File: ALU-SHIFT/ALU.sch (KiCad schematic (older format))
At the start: 55 parts, among them J1 Conn_01x02, J2 Conn_01x08, J3 Conn_01x08, J4 Conn_01x08, J5 Conn_01x04, J6 Conn_01x08, J7 Conn_01x02, U1 74LS08, U10 74LS245, U2 74LS245, U3 74LS08, U4 74LS32, U5 74LS86, U6 74LS245, U7 74LS32, U8 74LS245, U9 74LS86

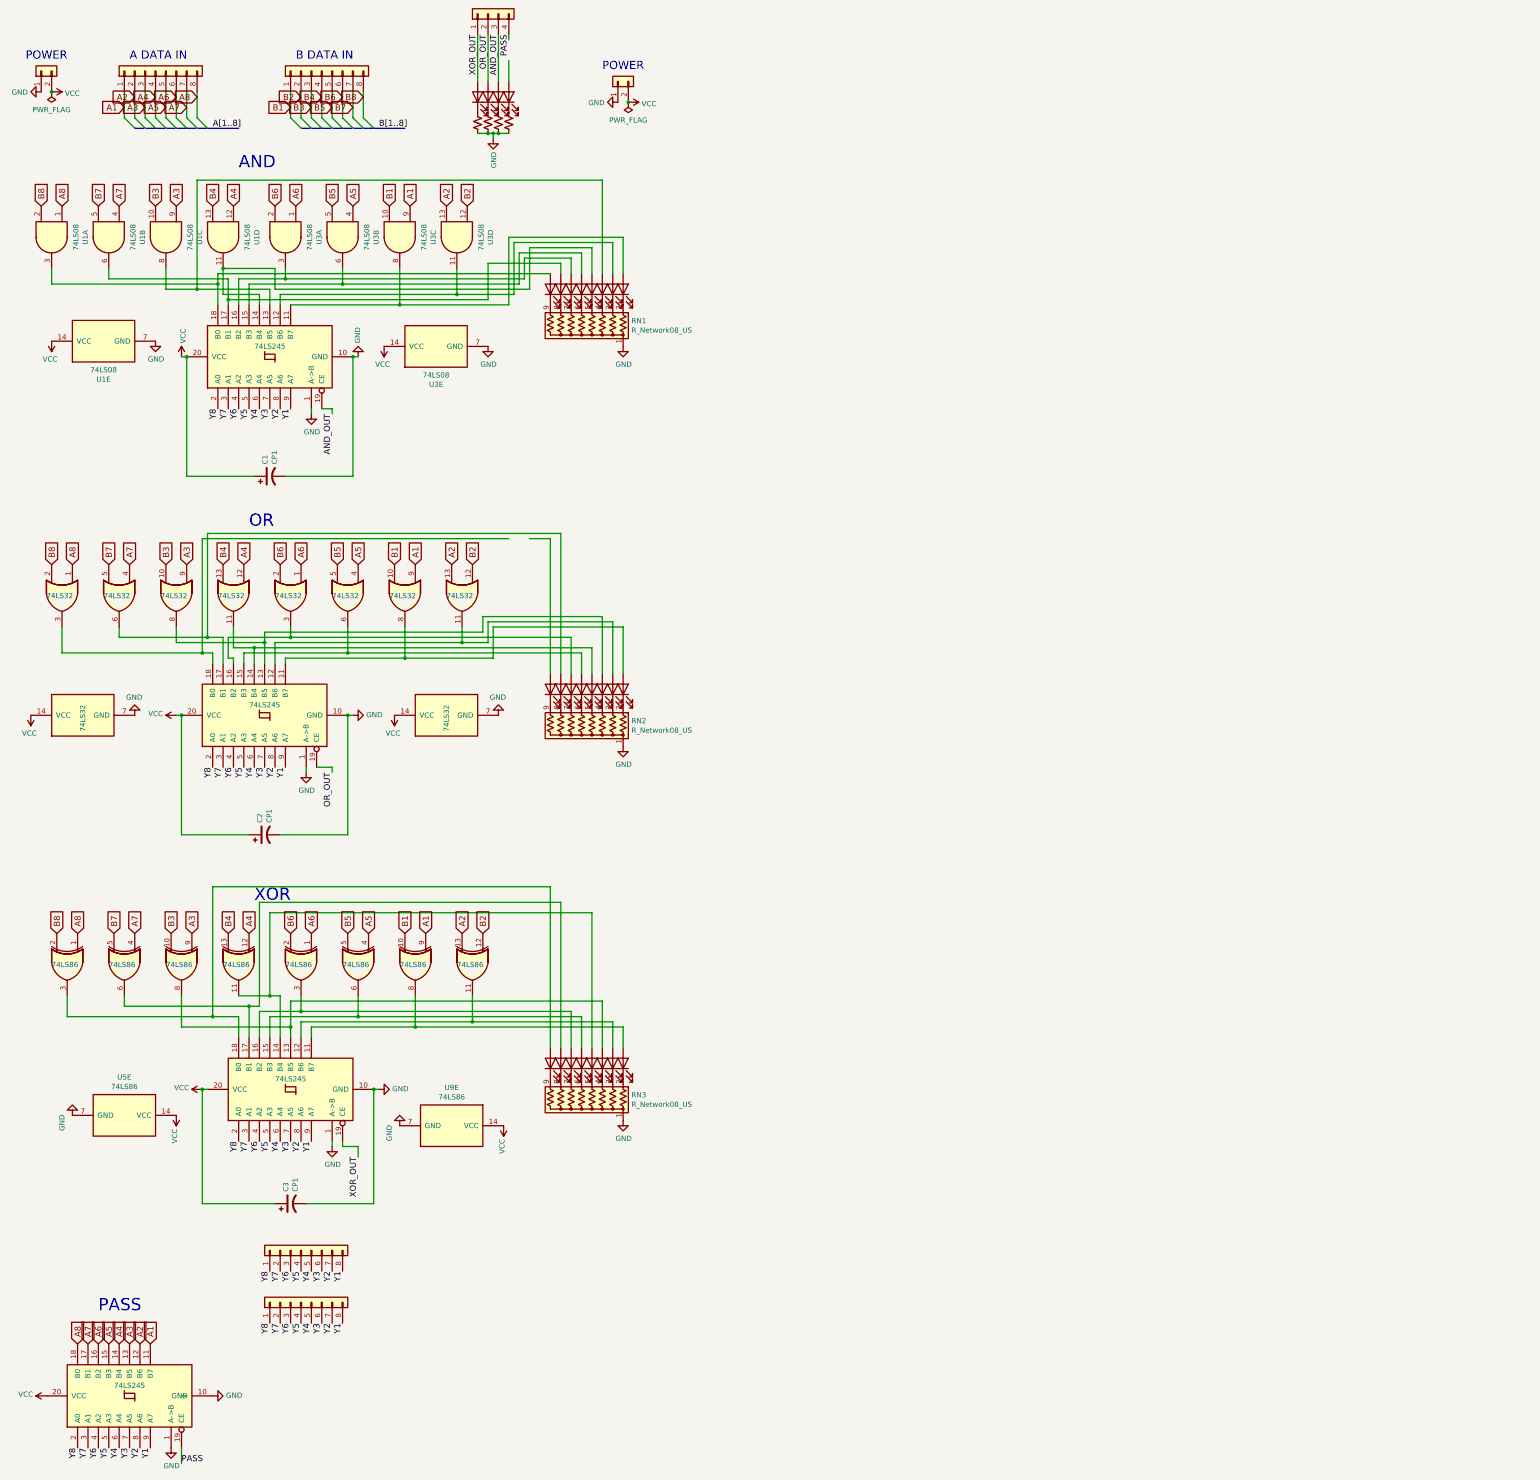
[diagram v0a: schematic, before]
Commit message: BiDirectional Shift Register component
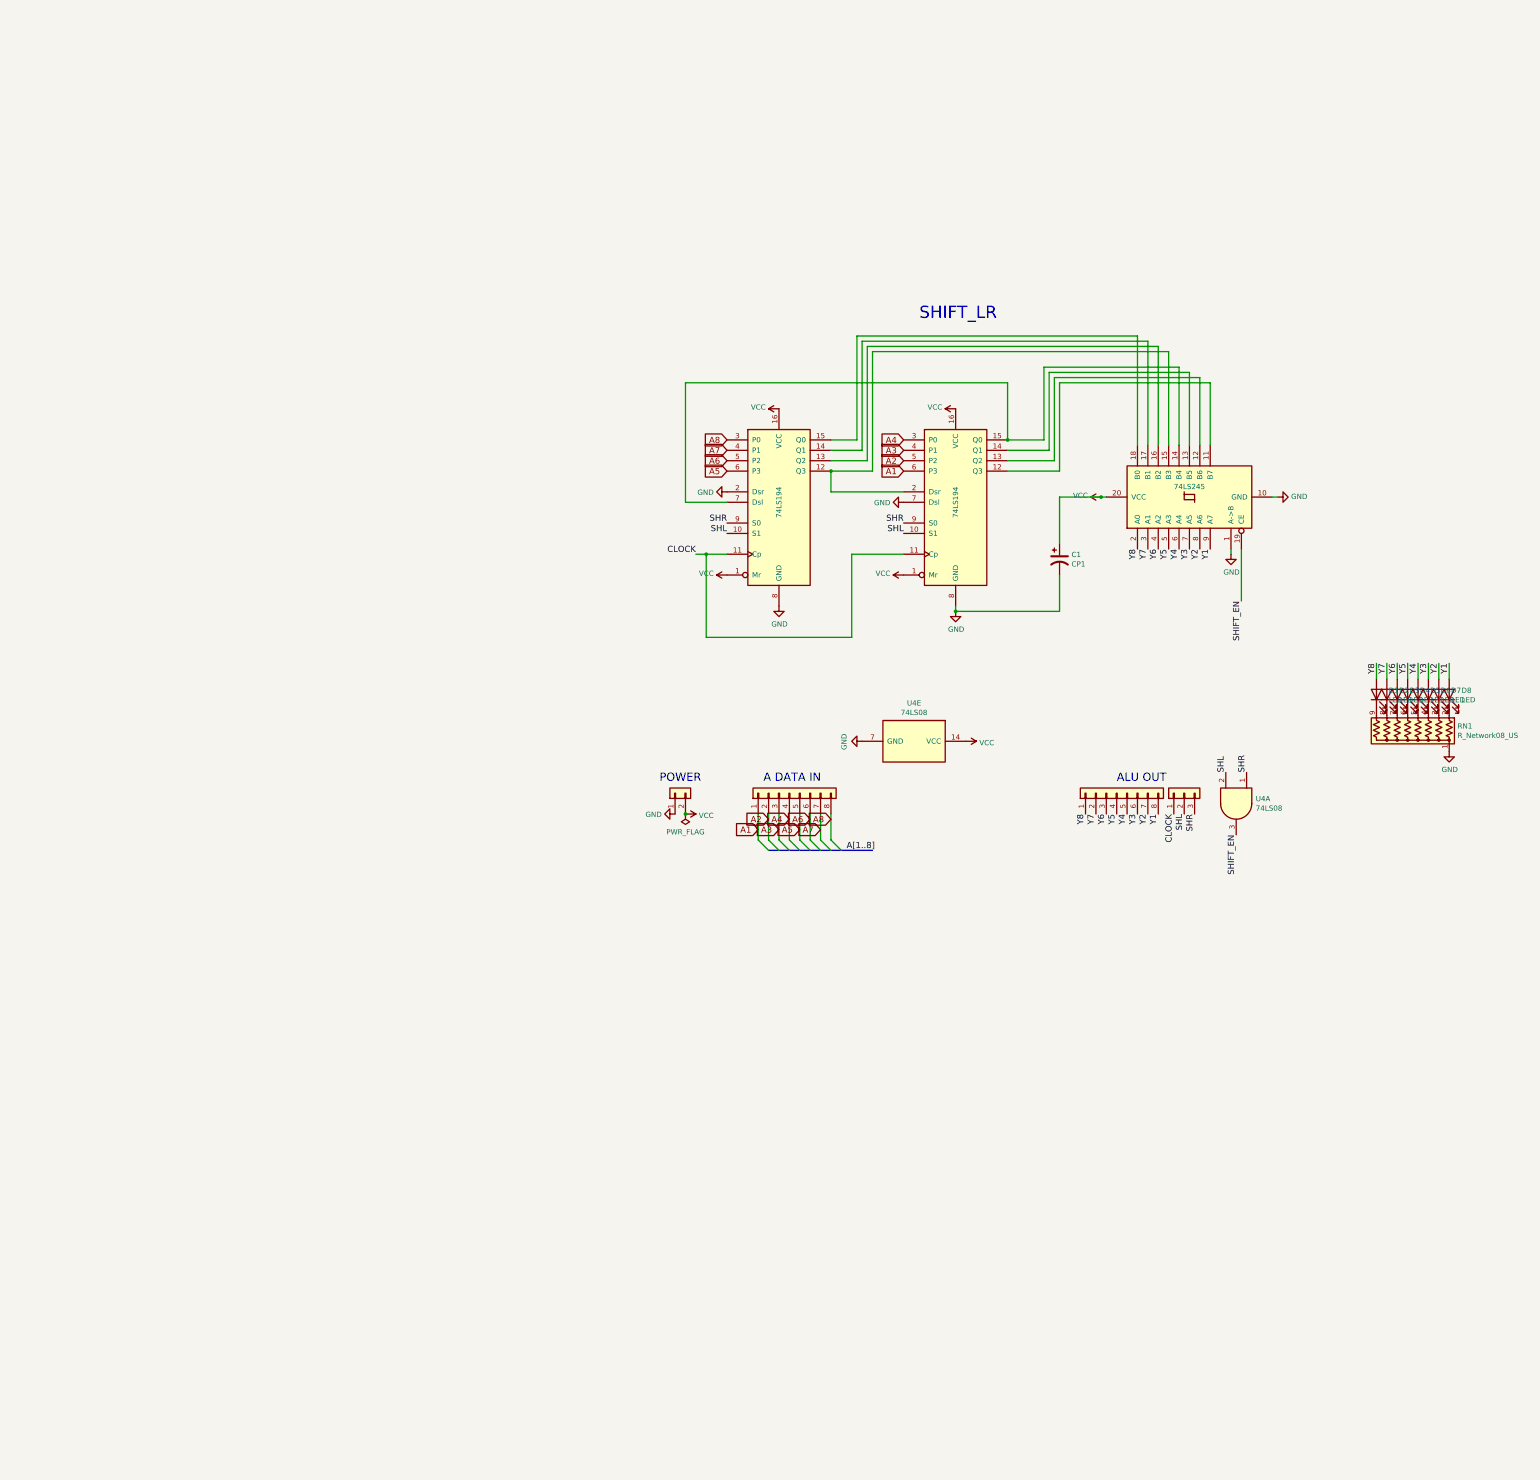
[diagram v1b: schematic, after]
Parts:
- removed C2, C3: CP1, Capacitor_THT:C_Radial_D6.3mm_H11.0mm_P2.50mm, symbol Device:CP1
- removed D10, D11, D12, D13, D14, D15, D16, D17, D18, D19, D20, D21, D22, D23, D24, D25, D26, D27, D28, D9: LED, LED_THT:LED_D5.0mm, symbol Device:LED
- removed J4, J6: Conn_01x08, Connector_PinHeader_2.54mm:PinHeader_1x08_P2.54mm_Vertical, symbol Connector_Generic:Conn_01x08
- removed J5: Conn_01x04, Connector_PinHeader_2.54mm:PinHeader_1x04_P2.54mm_Vertical, symbol Connector_Generic:Conn_01x04
- removed J7: Conn_01x02, Connector_PinHeader_2.54mm:PinHeader_1x02_P2.54mm_Vertical, symbol Connector_Generic:Conn_01x02
- removed R1, R2, R3, R4: R_Small_US, Resistor_THT:R_Axial_DIN0207_L6.3mm_D2.5mm_P10.16mm_Horizontal, symbol Device:R_Small_US
- removed RN2, RN3: R_Network08_US, Resistor_THT:R_Array_SIP9, symbol Device:R_Network08_US
- removed U1, U3: 74LS08, Package_DIP:DIP-14_W7.62mm, symbol 74xx:74LS08
- removed U10, U2, U6, U8: 74LS245, Package_DIP:DIP-20_W7.62mm, symbol 74xx:74LS245
- removed U4, U7: 74LS32, Package_DIP:DIP-14_W7.62mm, symbol 74xx:74LS32
- removed U5, U9: 74LS86, Package_DIP:DIP-14_W7.62mm, symbol 74xx:74LS86
- added J4: Conn_01x03, Connector_PinHeader_2.54mm:PinHeader_1x03_P2.54mm_Vertical, symbol Connector_Generic:Conn_01x03
- added U1, U2: 74LS194, Package_DIP:DIP-16_W7.62mm, symbol 74xx:74LS194
- added U3: 74LS245, Package_DIP:DIP-20_W7.62mm, symbol 74xx:74LS245
- added U4: 74LS08, Package_DIP:DIP-14_W7.62mm, symbol 74xx:74LS08
- D1, D2, D3, D4, D5, D6, D7, D8: footprint LED_THT:LED_D5.0mm -> LED_THT:LED_D3.0mm
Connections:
- net labels added: CLOCK, SHIFT_EN, SHL, SHR
- net labels removed: AND_OUT, B1, B2, B3, B4, B5, B6, B7, B8, B[1..8], OR_OUT, PASS, XOR_OUT
- wire segments 212 -> 69
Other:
- note added: "ALU OUT"
- note added: "SHIFT_LR"
- note removed: "AND"
- note removed: "B DATA IN"
- note removed: "OR"
- note removed: "PASS"
- note removed: "XOR"
